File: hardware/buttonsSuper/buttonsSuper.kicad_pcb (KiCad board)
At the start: 2 copper layers, 136.8 x 62 mm, 15 parts, among them U1 SKRBAKE010, U10 SKRBAKE010, U2 SKRBAKE010, U3 SKRBAKE010, U4 SKRBAKE010, U5 SKRBAKE010, U6 SKRBAKE010, U7 SKRBAKE010, U8 SKRBAKE010, U9 SKRBAKE010

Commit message: Latest
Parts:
- removed U1, U10, U2, U3, U4, U5, U6, U7, U8, U9: SKRBAKE010, JLCPCB_footprint:KEY-SMD_4P-L4.0-W4.8-P3.90-LS4.8
- added CIRCLE1: K2-1187SQ-E4SW-06, JLCPCB_footprint:KEY-SMD_4P-L5.2-W5.2-P3.70-LS6.4, F.Cu at (167.5, 94.3)
- added CROSS1: K2-1187SQ-E4SW-06, JLCPCB_footprint:KEY-SMD_4P-L5.2-W5.2-P3.70-LS6.4, F.Cu at (157.8, 104.2)
- added DOWN1: K2-1187SQ-E4SW-06, JLCPCB_footprint:KEY-SMD_4P-L5.2-W5.2-P3.70-LS6.4, F.Cu at (49.5, 117.8)
- added G***: LOGO, consolizer:logo_small, F.Cu at (131.8, 128.0)
- added G***: LOGO, consolizer:logo_small, F.Cu at (98.8, 105.0)
- added L1: K2-1187SQ-E4SW-06, JLCPCB_footprint:KEY-SMD_4P-L5.2-W5.2-P3.70-LS6.4, F.Cu at (47.8, 81.8)
- added LEFT1: K2-1187SQ-E4SW-06, JLCPCB_footprint:KEY-SMD_4P-L5.2-W5.2-P3.70-LS6.4, F.Cu at (42.0, 110.2)
- added R1: K2-1187SQ-E4SW-06, JLCPCB_footprint:KEY-SMD_4P-L5.2-W5.2-P3.70-LS6.4, F.Cu at (156.7, 65.8)
- added RIGHT1: K2-1187SQ-E4SW-06, JLCPCB_footprint:KEY-SMD_4P-L5.2-W5.2-P3.70-LS6.4, F.Cu at (57.0, 110.2)
- added SQUARE1: K2-1187SQ-E4SW-06, JLCPCB_footprint:KEY-SMD_4P-L5.2-W5.2-P3.70-LS6.4, F.Cu at (148.0, 94.5)
- added TRIANGLE1: K2-1187SQ-E4SW-06, JLCPCB_footprint:KEY-SMD_4P-L5.2-W5.2-P3.70-LS6.4, F.Cu at (157.5, 84.5)
- added UP1: K2-1187SQ-E4SW-06, JLCPCB_footprint:KEY-SMD_4P-L5.2-W5.2-P3.70-LS6.4, F.Cu at (49.5, 102.8)
- C1, C2: value trill-flex-conector_10 -> flex-conector_10
- C3: value trill-flex-conector_8_1 -> flex-conector_8_1
- C4: value trill-flex-conector_14 -> flex-conector_14
- C5: value trill-flex-conector_10 -> flex-conector_10; footprint consolizer:flex_short_10 -> consolizer:flex_long_10; moved to B.Cu
- moved C5 167.2 mm to (67.5, 105.2), turned to -90 degrees
- moved C3 75.2 mm to (150.4, 117.5), turned to 90 degrees
- moved C4 39.0 mm to (110.1, 93.1)
- moved C2 35.8 mm to (73.5, 118.0)
- moved C1 22.3 mm to (160.5, 128.2)
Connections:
- C3 pad 1: unconnected-(C3-Pad1) -> /gnd
- C3 pad 2: /five -> /gnd
- C3 pad 3: /four -> /one
- C3 pad 4: /three -> /tw
- C3 pad 5: /tw -> /three
- C3 pad 6: /one -> /four
- C3 pad 7: /gnd -> /five
- C3 pad 8: /gnd -> unconnected-(C3-Pad8)
- C4 pad 1: /Square -> /five
- C4 pad 10: /one -> /cross
- C4 pad 11: /tw -> /Circle
- C4 pad 12: /three -> /Triangle
- C4 pad 13: /four -> /R1
- C4 pad 14: /five -> /Square
- C4 pad 2: /R1 -> /four
- C4 pad 3: /Triangle -> /three
- C4 pad 4: /Circle -> /tw
- C4 pad 5: /cross -> /one
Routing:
- net GND: track 257.5 -> 333.8 mm, vias 2 -> 5
- net /Square: track 161.9 -> 124.4 mm, vias 3 -> 1
- net /R1: track 215.2 -> 181.1 mm, vias 2 -> 1
- net /gnd: track 304.6 -> 336.6 mm, vias 2 -> 3
- net /Circle: track 130.7 -> 156.9 mm, vias 2 -> 1
- net /left: track 142.1 -> 160.6 mm, vias 4 -> 2
- net /up: track 142.4 -> 159.3 mm, vias 4 -> 2
- net /Triangle: track 170.5 -> 156.9 mm, vias 2 -> 1
- net /l1: track 158.1 -> 170.3 mm
- net /right: track 124.8 -> 136.3 mm
- net /down: track 134.2 -> 144.2 mm, vias 4 -> 2
- net /cross: track 144.8 -> 140.6 mm, vias 2 -> 1
- net /three: track 60.6 -> 59.8 mm
- net /five: track 60.6 -> 59.9 mm
- net /one: track 60.6 -> 59.8 mm
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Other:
- board size 136.8 x 62 mm -> 137.2 x 70.8 mm
- board text added: "A"
- board text added: "B"
- board text added: "PSP"

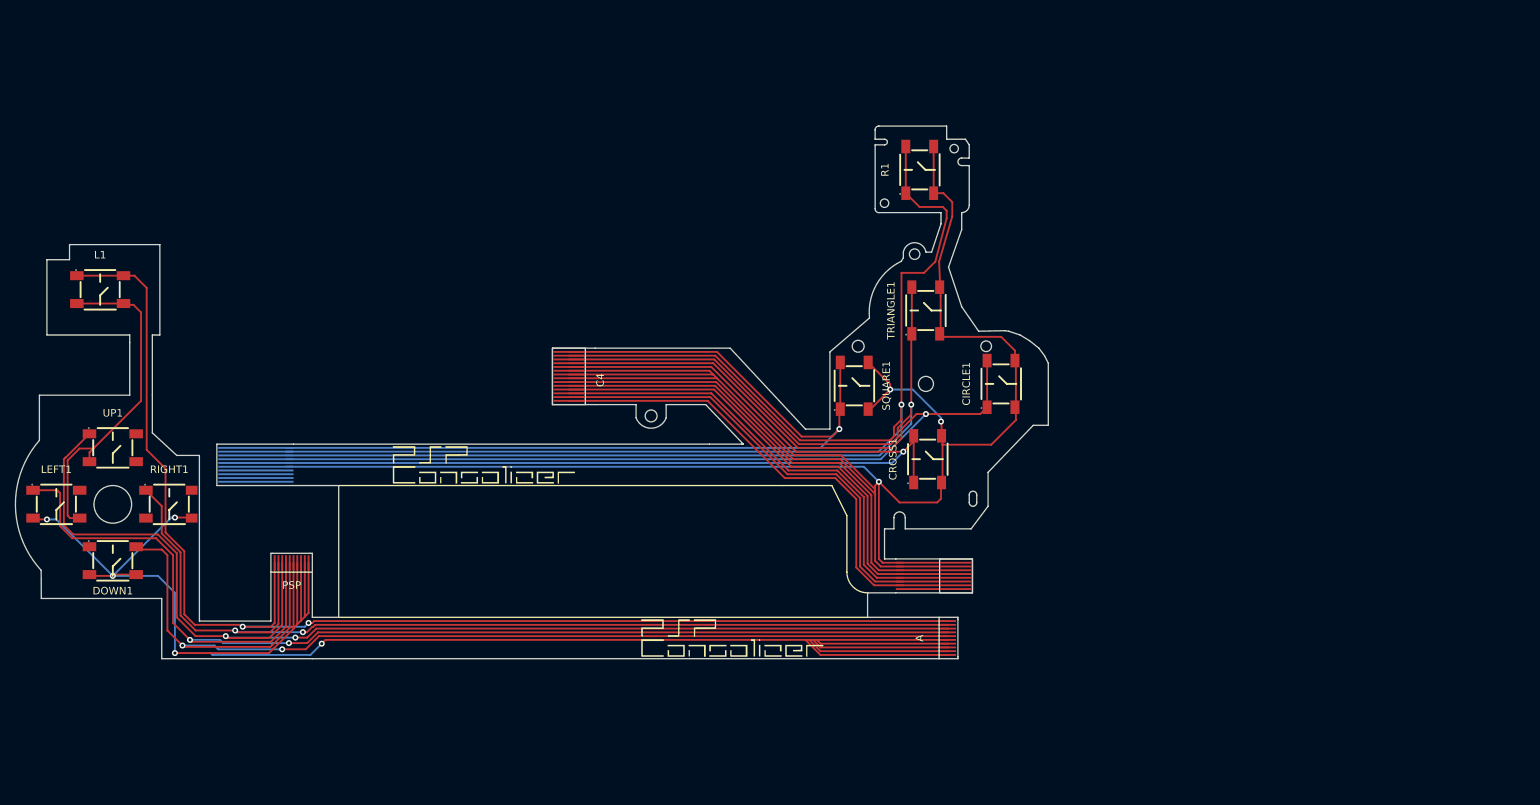
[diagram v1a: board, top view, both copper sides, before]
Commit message: Added analog stick
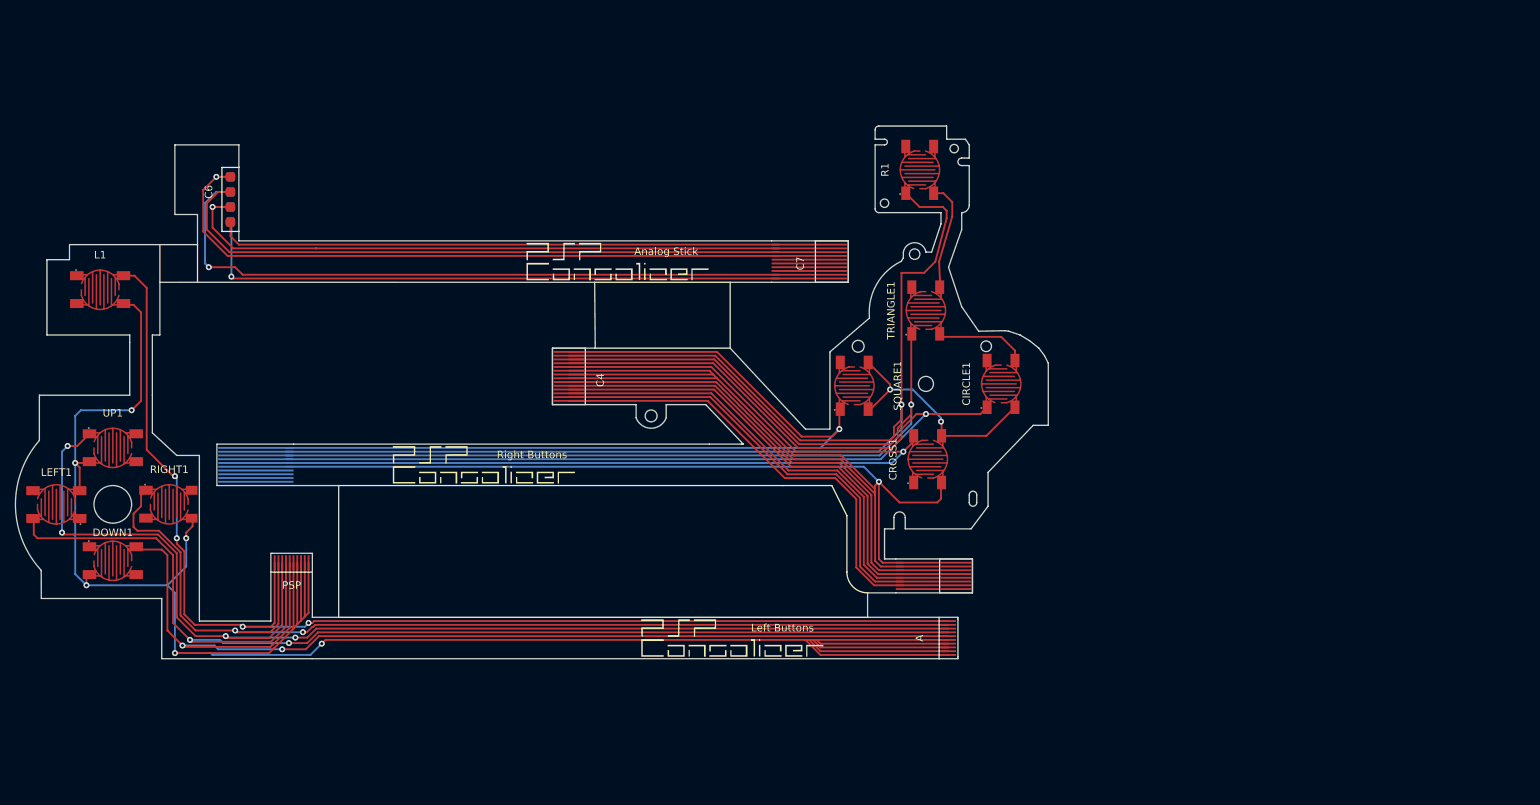
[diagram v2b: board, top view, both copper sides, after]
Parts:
- added C6: PSP-analog, consolizer:PSP-analog, F.Cu at (65.2, 69.0)
- added C7: flex-conector_10, consolizer:flex_long_10, F.Cu at (143.0, 78.2)
- added G***: LOGO, consolizer:logo_small, F.Cu at (116.5, 78.0)
- CIRCLE1, CROSS1, DOWN1, L1, LEFT1, R1, RIGHT1, SQUARE1, TRIANGLE1, UP1: footprint JLCPCB_footprint:KEY-SMD_4P-L5.2-W5.2-P3.70-LS6.4 -> JLCPCB_footprint:KEY-SMD_4P-L5.2-W5.2-P3.70-LS6.4_1
- turned LEFT1 to 180 degrees
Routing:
- net /X_2: track 0.00 -> 88.9 mm, vias 0 -> 1
- net /X_1: track 0.00 -> 84.5 mm
- net /+v: track 0.00 -> 83.9 mm, vias 0 -> 1
- net /Y_2: track 0.00 -> 80.2 mm, vias 0 -> 1
- net GND: track 333.8 -> 412.9 mm, vias 5 -> 7
- net /Y_1: track 0.00 -> 75.2 mm
- net /gnd: track 336.6 -> 312.8 mm
- net /cross: track 140.6 -> 134.4 mm
- net /Square: track 124.4 -> 118.2 mm
- net /R1: track 181.1 -> 174.9 mm
- net /Circle: track 156.9 -> 150.7 mm
- net /Triangle: track 156.9 -> 150.7 mm
- net /l1: track 170.3 -> 164.3 mm, vias 2 -> 4
- net /right: track 136.3 -> 139.4 mm
- net /left: track 160.6 -> 157.9 mm
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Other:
- outline, holes or cut-outs redrawn
- board text added: "Analog Stick"
- board text added: "Left Buttons"
- board text added: "Right Buttons"

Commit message: changes im not sure about, need to figure out what it is all about
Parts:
- moved G*** 29.7 mm to (144.5, 68.0), turned to 90 degrees
- moved C7 28.8 mm to (144.8, 49.5), turned to 0 degrees
- moved G*** 13.8 mm to (145.5, 128.0)
- moved G*** 11.8 mm to (87.0, 105.0)
- moved C6 5.25 mm to (65.4, 74.3)
- moved R1 2.62 mm to (156.7, 63.2)
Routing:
- net /Y_2: track 80.2 -> 119.3 mm
- net /X_2: track 88.9 -> 126.8 mm
- net GND: track 412.9 -> 447.2 mm
- net /X_1: track 84.5 -> 116.4 mm
- net /Y_1: track 75.2 -> 106.0 mm
- net /+v: track 83.9 -> 113.9 mm
- net /up: track 161.0 -> 168.2 mm
- net /l1: track 164.3 -> 168.8 mm
- net /gnd: track 312.8 -> 315.4 mm
- net /R1: track 174.9 -> 177.5 mm
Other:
- board size 137.2 x 70.8 mm -> 137.2 x 75.3 mm
- board text added: "Stiffener: Polyimide Stiffener thickness: 0.2mm Stiffener Location: Refer to User.Drawings layer This is intended to be manufactured as a single board, not as three individual boards. Thanks :)"
- board text removed: "B"
- board text removed: "PSP"
